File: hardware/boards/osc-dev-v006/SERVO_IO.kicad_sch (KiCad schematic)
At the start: 7 parts, among them J4 JST-ZH-H, J5 PIN-V, J6 PIN-V

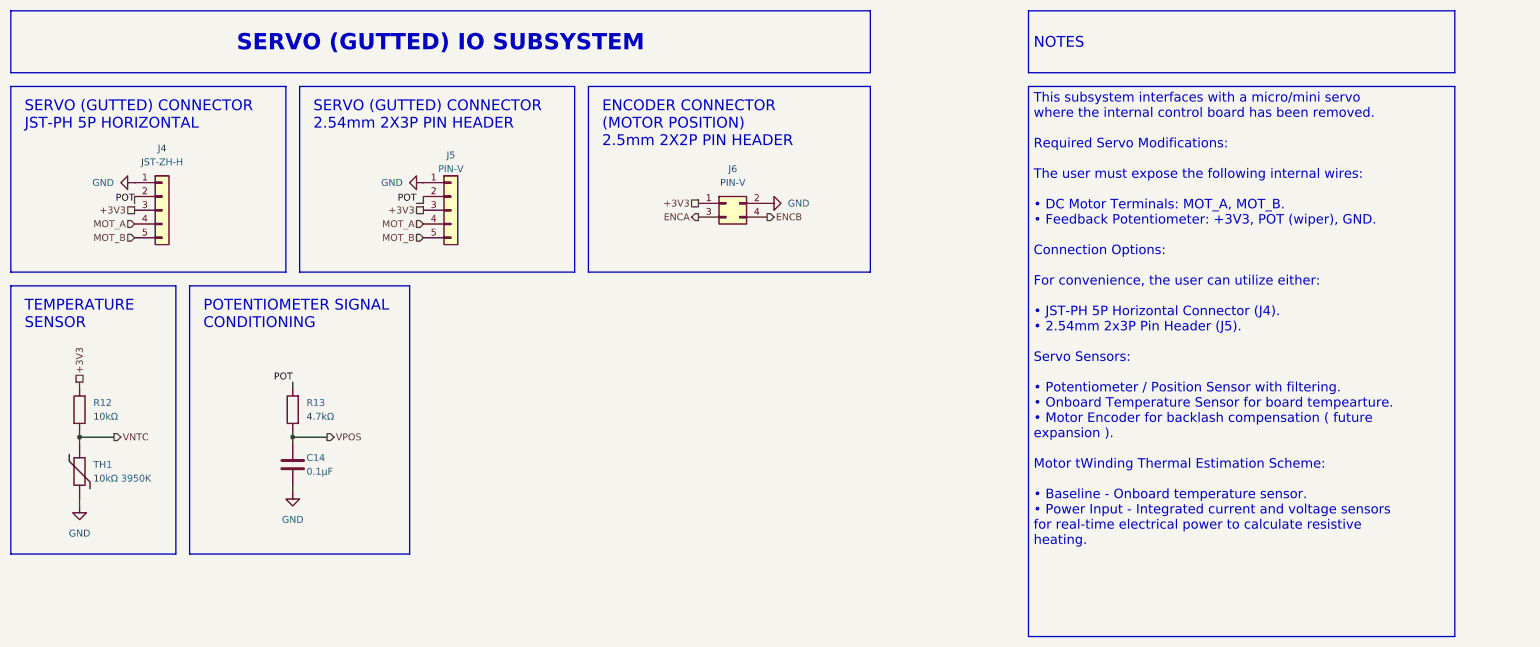
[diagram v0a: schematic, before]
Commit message: OSC DEV CH32 REV B (#10)
* update board

* updated schematics. ERC on schematics is now passing

* completed routing.

* adding ground vias

* update schematics notes

* update bom and component properties

* use red header pins for jumpers

* rename board to osc-dev-v006

* add docs
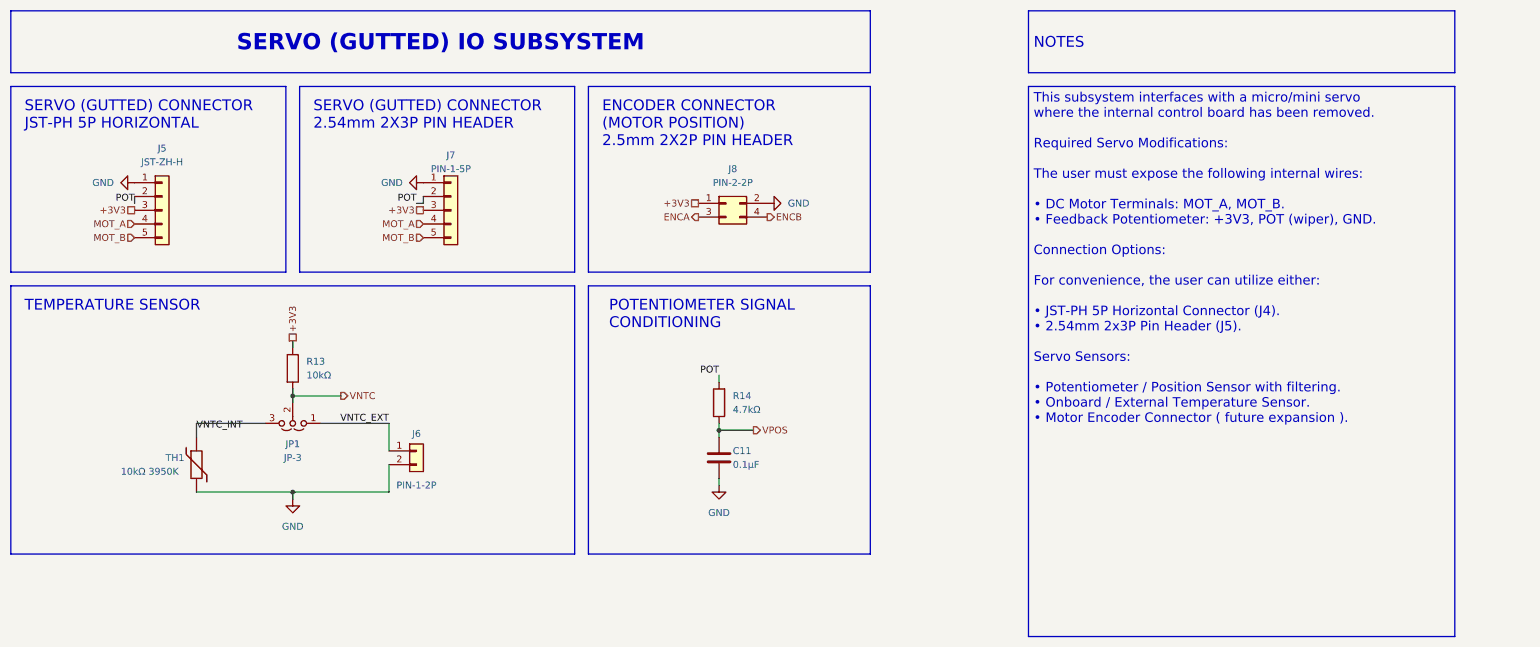
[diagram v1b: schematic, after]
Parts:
- removed R12: 10kΩ, Resistor_SMD:R_0805_2012Metric_Pad1.20x1.40mm_HandSolder, symbol Device:R
- added J6: PIN-1-2P, Connector_PinHeader_2.54mm:PinHeader_1x02_P2.54mm_Vertical, symbol Connector_Generic:Conn_01x02
- added JP1: JP-3, Connector_PinHeader_2.54mm:PinHeader_1x03_P2.54mm_Vertical, symbol Jumper:Jumper_3_Open
- added R13: 10kΩ, Resistor_SMD:R_0805_2012Metric_Pad1.20x1.40mm_HandSolder, symbol Device:R
- J7: renamed from J5; value PIN-V -> PIN-1-5P
- J8: renamed from J6; value PIN-V -> PIN-2-2P
- renumbered C14 to C11, J4 to J5, R13 to R14
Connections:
- net +3V3: now also R13.1
- net GND: now also J6.2 (Pin_2)
- net VNTC: now also JP1.2 (C), R13.2; no longer TH1.1
- new net VNTC_EXT: J6.1 (Pin_1), JP1.1 (A)
- new net VNTC_INT: JP1.3 (B), TH1.1
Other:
- moved on the sheet: C11, R14, TH1
